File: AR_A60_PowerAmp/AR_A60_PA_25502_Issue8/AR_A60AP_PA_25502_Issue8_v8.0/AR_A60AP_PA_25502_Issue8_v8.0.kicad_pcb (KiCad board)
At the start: 2 copper layers, 128.3 x 90.2 mm, 83 parts, among them J1 Conn_01x04, J2 J_HP+, Q10 BC547, Q11 BC547, Q12 BC547, Q13 ZTX753, Q14 BC547, Q15 ZTX653, Q16 BC547, Q17 BC557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

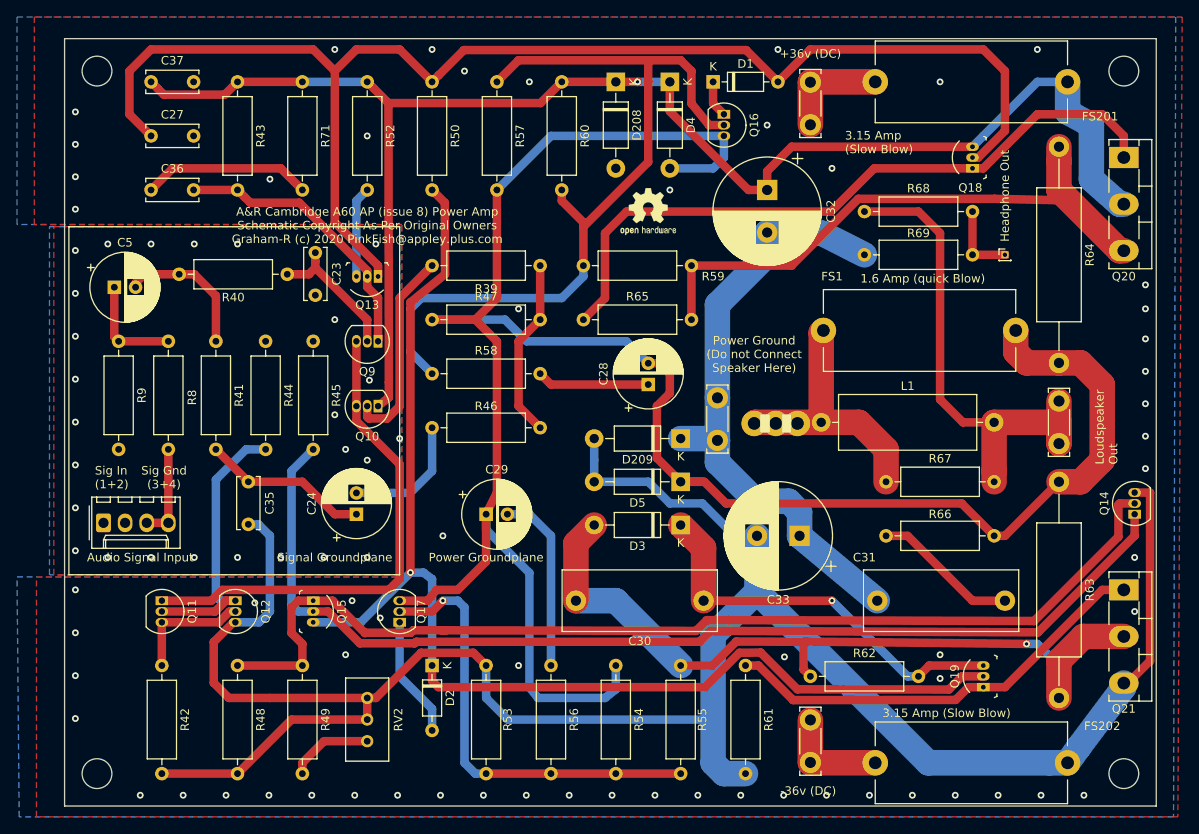
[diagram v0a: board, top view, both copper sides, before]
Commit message: Updated polycarb caps
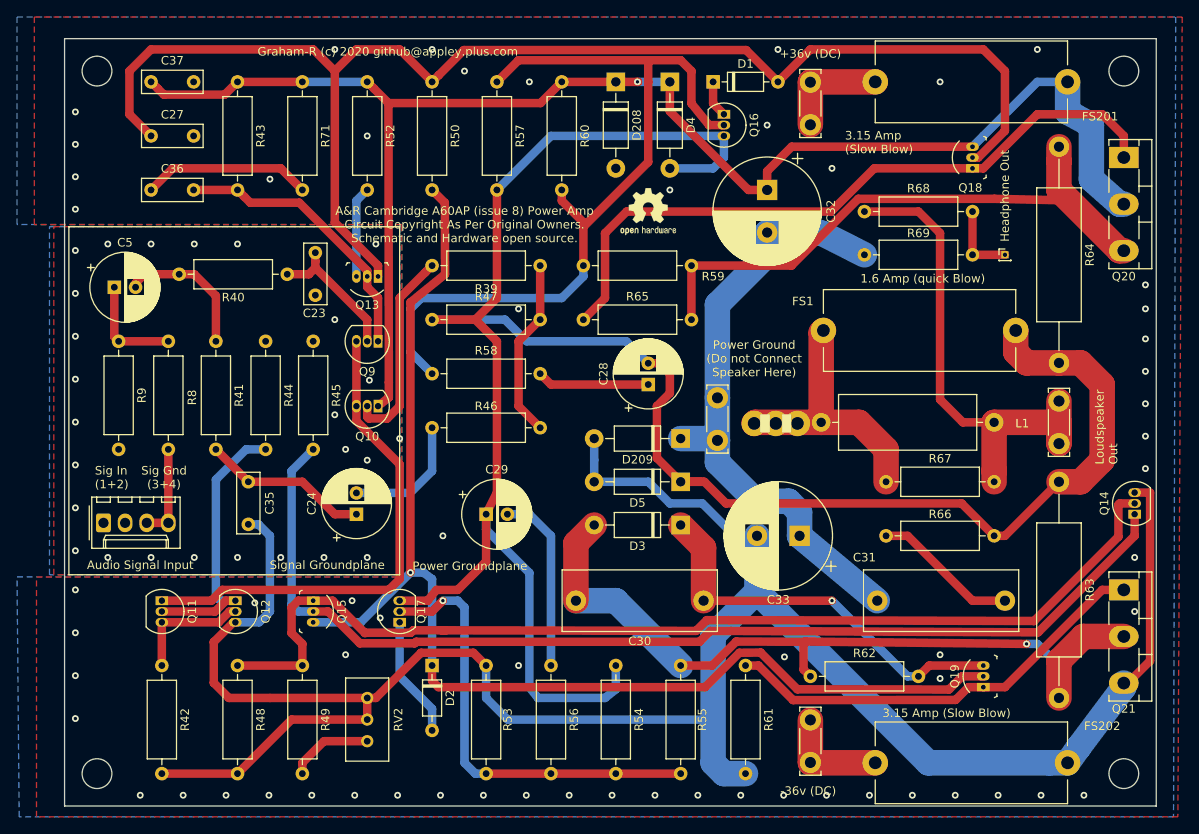
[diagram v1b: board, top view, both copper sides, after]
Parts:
- C23, C27, C35, C36, C37: footprint Capacitor_THT:C_Disc_D6.0mm_W2.5mm_P5.00mm -> Capacitor_THT:C_Rect_L7.0mm_W2.5mm_P5.00mm
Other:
- board text added: "A&R Cambridge A60AP (issue 8) Power Amp Circuit Copyright As Per Original Owners. Schematic and Hardware open source."
- board text added: "Graham-R (c) 2020 github@appley.plus.com"
- board text removed: "A&R Cambridge A60 AP (issue 8) Power Amp Schematic Copyright As Per Original Owners Graham-R (c) 2020 PinkFish@appley.plus.com"
